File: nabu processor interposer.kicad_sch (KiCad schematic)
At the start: 4 parts

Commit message: changed bus names to avoid possible conflicts, fixed unnamed busses.
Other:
- sheet MAPPER ports: added PAB_{1}_{[0..7]}, PAB_{2}_{[0..7]}, PAB_{3}_{[0..7]}, PAB_{4}_{[0..7]}; removed PAN_{1}_{[0..7]}, PAN_{2}_{[0..7]}, PAN_{3}_{[0..7]}, PAN_{4}_{[0..7]}
- sheet MUX ports: added PAB_{1}_{[0..7]}, PAB_{2}_{[0..7]}, PAB_{3}_{[0..7]}, PAB_{4}_{[0..7]}; removed PAN_{1}_{[0..7]}, PAN_{2}_{[0..7]}, PAN_{3}_{[0..7]}, PAN_{4}_{[0..7]}
- sheet RESET ports: added PABI_{1}_{[0..7]}, PABI_{2}_{[0..7]}, PABI_{3}_{[0..7]}, PABI_{4}_{[0..7]}, PABO_{1}_{[0..7]}, PABO_{2}_{[0..7]}, PABO_{3}_{[0..7]}, PABO_{4}_{[0..7]}; removed PANI_{1}_{[0..7]}, PANI_{2}_{[0..7]}, PANI_{3}_{[0..7]}, PANI_{4}_{[0..7]}, PANO_{1}_{[0..7]}, PANO_{2}_{[0..7]}, PANO_{3}_{[0..7]}, PANO_{4}_{[0..7]}
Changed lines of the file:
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@@
       (effects (font (size 1.27 1.27)) (justify left top))
     )
-    (pin "PAN_{4}_{[0..7]}" input (at 177.8 53.34 180)
-      (effects (font (size 1.27 1.27)) (justify left))
-    )
-    (pin "PAN_{1}_{[0..7]}" input (at 177.8 60.96 180)
-      (effects (font (size 1.27 1.27)) (justify left))
-    )
-    (pin "PAN_{2}_{[0..7]}" input (at 177.8 58.42 180)
-      (effects (font (size 1.27 1.27)) (justify left))
-    )
-    (pin "PAN_{3}_{[0..7]}" input (at 177.8 55.88 180)
+    (pin "PAB_{4}_{[0..7]}" input (at 177.8 53.34 180)
+      (effects (font (size 1.27 1.27)) (justify left))
+    )
+    (pin "PAB_{1}_{[0..7]}" input (at 177.8 60.96 180)
+      (effects (font (size 1.27 1.27)) (justify left))
+    )
+    (pin "PAB_{2}_{[0..7]}" input (at 177.8 58.42 180)
+      (effects (font (size 1.27 1.27)) (justify left))
+    )
+    (pin "PAB_{3}_{[0..7]}" input (at 177.8 55.88 180)
       (effects (font (size 1.27 1.27)) (justify left))
     )
@@
       (effects (font (size 1.27 1.27)) (justify left))
     )
-    (pin "PAN_{2}_{[0..7]}" output (at 127 58.42 0)
-      (effects (font (size 1.27 1.27)) (justify right))
-    )
-    (pin "PAN_{3}_{[0..7]}" output (at 127 55.88 0)
-      (effects (font (size 1.27 1.27)) (justify right))
-    )
-    (pin "PAN_{4}_{[0..7]}" output (at 127 53.34 0)
-      (effects (font (size 1.27 1.27)) (justify right))
-    )
-    (pin "PAN_{1}_{[0..7]}" output (at 127 60.96 0)
+    (pin "PAB_{2}_{[0..7]}" output (at 127 58.42 0)
+      (effects (font (size 1.27 1.27)) (justify right))
+    )
+    (pin "PAB_{3}_{[0..7]}" output (at 127 55.88 0)
+      (effects (font (size 1.27 1.27)) (justify right))
+    )
+    (pin "PAB_{4}_{[0..7]}" output (at 127 53.34 0)
+      (effects (font (size 1.27 1.27)) (justify right))
+    )
+    (pin "PAB_{1}_{[0..7]}" output (at 127 60.96 0)
       (effects (font (size 1.27 1.27)) (justify right))
     )
@@
       (effects (font (size 1.27 1.27)) (justify left))
     )
-    (pin "PANO_{1}_{[0..7]}" output (at 165.1 60.96 0)
-      (effects (font (size 1.27 1.27)) (justify right))
-    )
-    (pin "PANI_{2}_{[0..7]}" input (at 139.7 58.42 180)
-      (effects (font (size 1.27 1.27)) (justify left))
-    )
-    (pin "PANI_{1}_{[0..7]}" input (at 139.7 60.96 180)
+    (pin "PABO_{1}_{[0..7]}" output (at 165.1 60.96 0)
+      (effects (font (size 1.27 1.27)) (justify right))
+    )
+    (pin "PABI_{2}_{[0..7]}" input (at 139.7 58.42 180)
+      (effects (font (size 1.27 1.27)) (justify left))
+    )
+    (pin "PABI_{1}_{[0..7]}" input (at 139.7 60.96 180)
       (effects (font (size 1.27 1.27)) (justify left))
     )
@@
       (effects (font (size 1.27 1.27)) (justify left))
     )
-    (pin "PANI_{3}_{[0..7]}" input (at 139.7 55.88 180)
-      (effects (font (size 1.27 1.27)) (justify left))
-    )
-    (pin "PANO_{2}_{[0..7]}" output (at 165.1 58.42 0)
+    (pin "PABI_{3}_{[0..7]}" input (at 139.7 55.88 180)
+      (effects (font (size 1.27 1.27)) (justify left))
+    )
+    (pin "PABO_{2}_{[0..7]}" output (at 165.1 58.42 0)
       (effects (font (size 1.27 1.27)) (justify right))
     )
@@
       (effects (font (size 1.27 1.27)) (justify left))
     )
-    (pin "PANO_{3}_{[0..7]}" output (at 165.1 55.88 0)
-      (effects (font (size 1.27 1.27)) (justify right))
-    )
-    (pin "PANI_{4}_{[0..7]}" input (at 139.7 53.34 180)
-      (effects (font (size 1.27 1.27)) (justify left))
-    )
-    (pin "PANO_{4}_{[0..7]}" output (at 165.1 53.34 0)
+    (pin "PABO_{3}_{[0..7]}" output (at 165.1 55.88 0)
+      (effects (font (size 1.27 1.27)) (justify right))
+    )
+    (pin "PABI_{4}_{[0..7]}" input (at 139.7 53.34 180)
+      (effects (font (size 1.27 1.27)) (justify left))
+    )
+    (pin "PABO_{4}_{[0..7]}" output (at 165.1 53.34 0)
       (effects (font (size 1.27 1.27)) (justify right))
     )
@@
       (reference "#PWR?") (unit 1) (value "GNDD") (footprint "")
     )
+    (path "/a56bd835-5210-4a5d-913a-91f46ae9d0de/4444ae02-e20d-484d-ba01-fc54cdd7c1b8"
+      (reference "#PWR?") (unit 1) (value "GNDD") (footprint "")
+    )
     (path "/a56bd835-5210-4a5d-913a-91f46ae9d0de/4590a333-d4d6-4e6e-8569-bd58a5425e31"
       (reference "#PWR?") (unit 1) (value "GNDD") (footprint "")
@@
       (reference "#PWR?") (unit 1) (value "GNDD") (footprint "")
     )
+    (path "/a56bd835-5210-4a5d-913a-91f46ae9d0de/788e5535-7fdd-4e12-a7a4-64e1762d5b7e"
+      (reference "#PWR?") (unit 1) (value "GNDD") (footprint "")
+    )

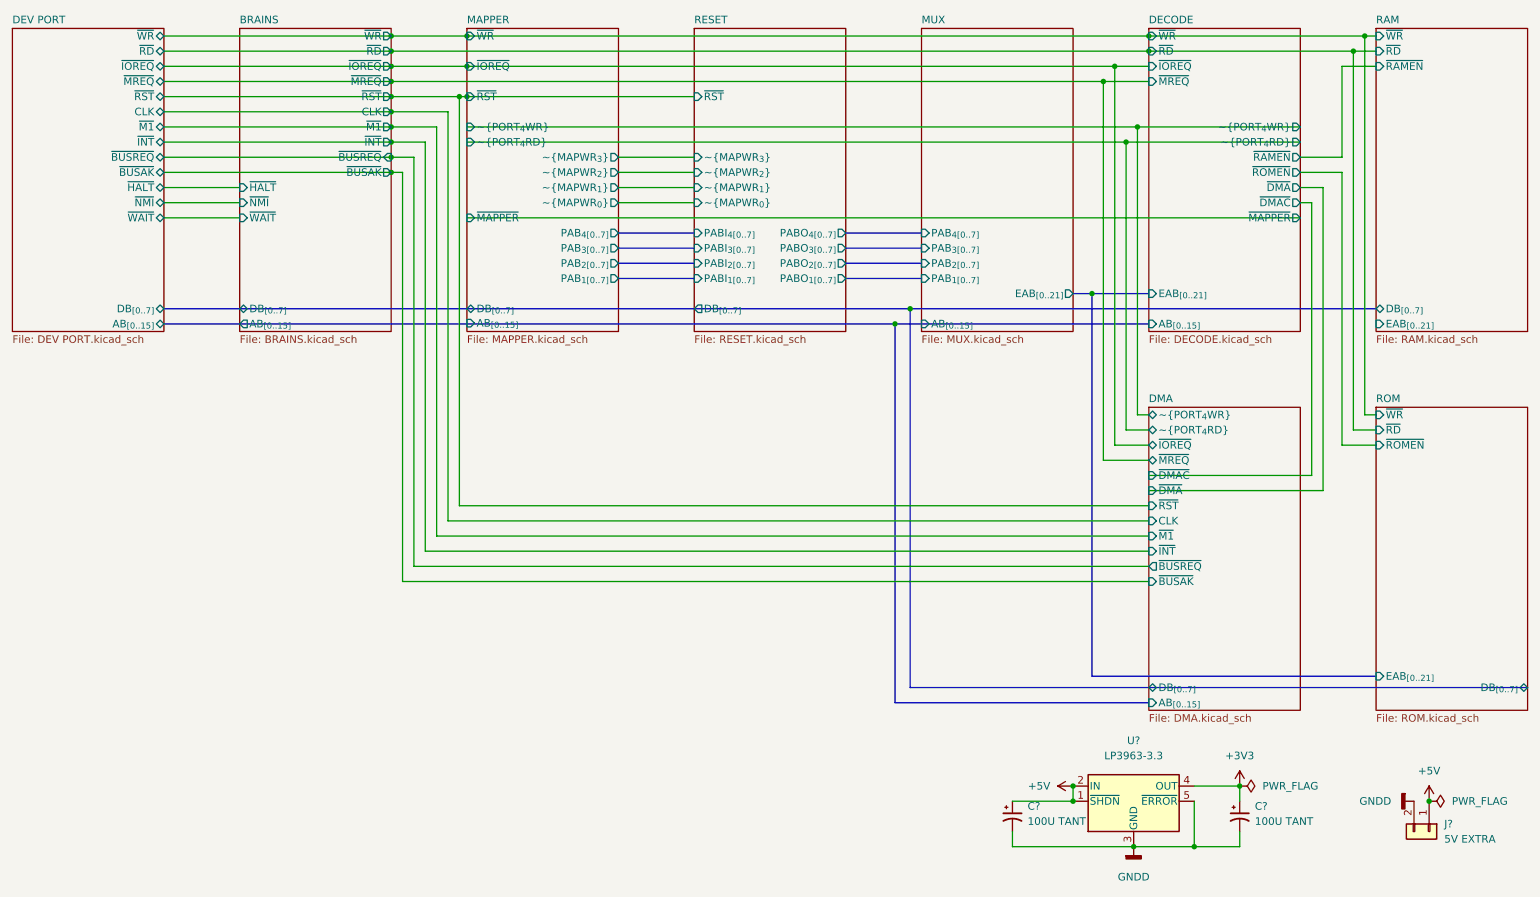
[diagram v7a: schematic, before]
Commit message: some clean up and simplification, as well as some renaming
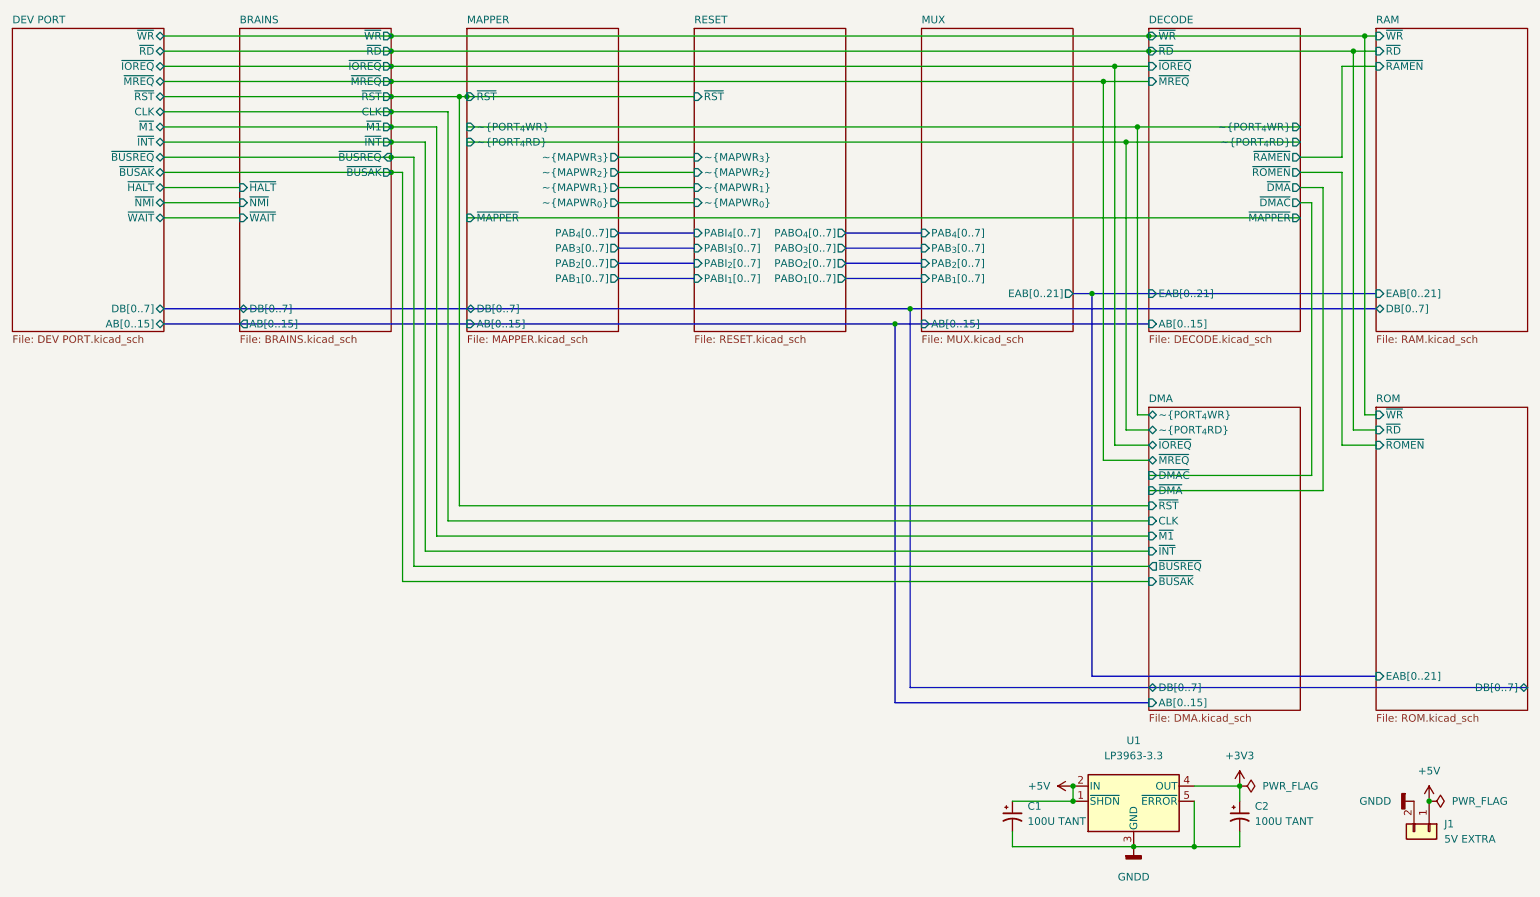
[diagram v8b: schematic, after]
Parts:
- gave numbers to parts that had none: 4
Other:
- sheet BRAINS ports: added AB[0..15], DB[0..7]; removed AB_{[0..15]}, DB_{[0..7]}
- sheet DECODE ports: added AB[0..15], EAB[0..21]; removed AB_{[0..15]}, EAB_{[0..21]}
- sheet DEV PORT ports: added AB[0..15], DB[0..7]; removed AB_{[0..15]}, DB_{[0..7]}
- sheet DMA ports: added AB[0..15], DB[0..7]; removed AB_{[0..15]}, DB_{[0..7]}
- sheet MAPPER ports: added AB[0..15], DB[0..7], PAB_{1}[0..7], PAB_{2}[0..7], PAB_{3}[0..7], PAB_{4}[0..7]; removed AB_{[0..15]}, DB_{[0..7]}, PAB_{1}_{[0..7]}, PAB_{2}_{[0..7]}, PAB_{3}_{[0..7]}, PAB_{4}_{[0..7]}, ~{IOREQ}, ~{WR}
- sheet MUX ports: added AB[0..15], EAB[0..21], PAB_{1}[0..7], PAB_{2}[0..7], PAB_{3}[0..7], PAB_{4}[0..7]; removed AB_{[0..15]}, EAB_{[0..21]}, PAB_{1}_{[0..7]}, PAB_{2}_{[0..7]}, PAB_{3}_{[0..7]}, PAB_{4}_{[0..7]}
- sheet RAM ports: added DB[0..7], EAB[0..21]; removed DB_{[0..7]}, EAB_{[0..21]}
- sheet RESET ports: added PABI_{1}[0..7], PABI_{2}[0..7], PABI_{3}[0..7], PABI_{4}[0..7], PABO_{1}[0..7], PABO_{2}[0..7], PABO_{3}[0..7], PABO_{4}[0..7]; removed DB_{[0..7]}, PABI_{1}_{[0..7]}, PABI_{2}_{[0..7]}, PABI_{3}_{[0..7]}, PABI_{4}_{[0..7]}, PABO_{1}_{[0..7]}, PABO_{2}_{[0..7]}, PABO_{3}_{[0..7]}, PABO_{4}_{[0..7]}
- sheet ROM ports: added DB[0..7], EAB[0..21]; removed DB_{[0..7]}, EAB_{[0..21]}
